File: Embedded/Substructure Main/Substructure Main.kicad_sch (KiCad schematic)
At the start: 12 parts, among them J1 M Pins, J2 C Pins, U1 G0 FFC, U2 G1 FFC, U3 S FFC

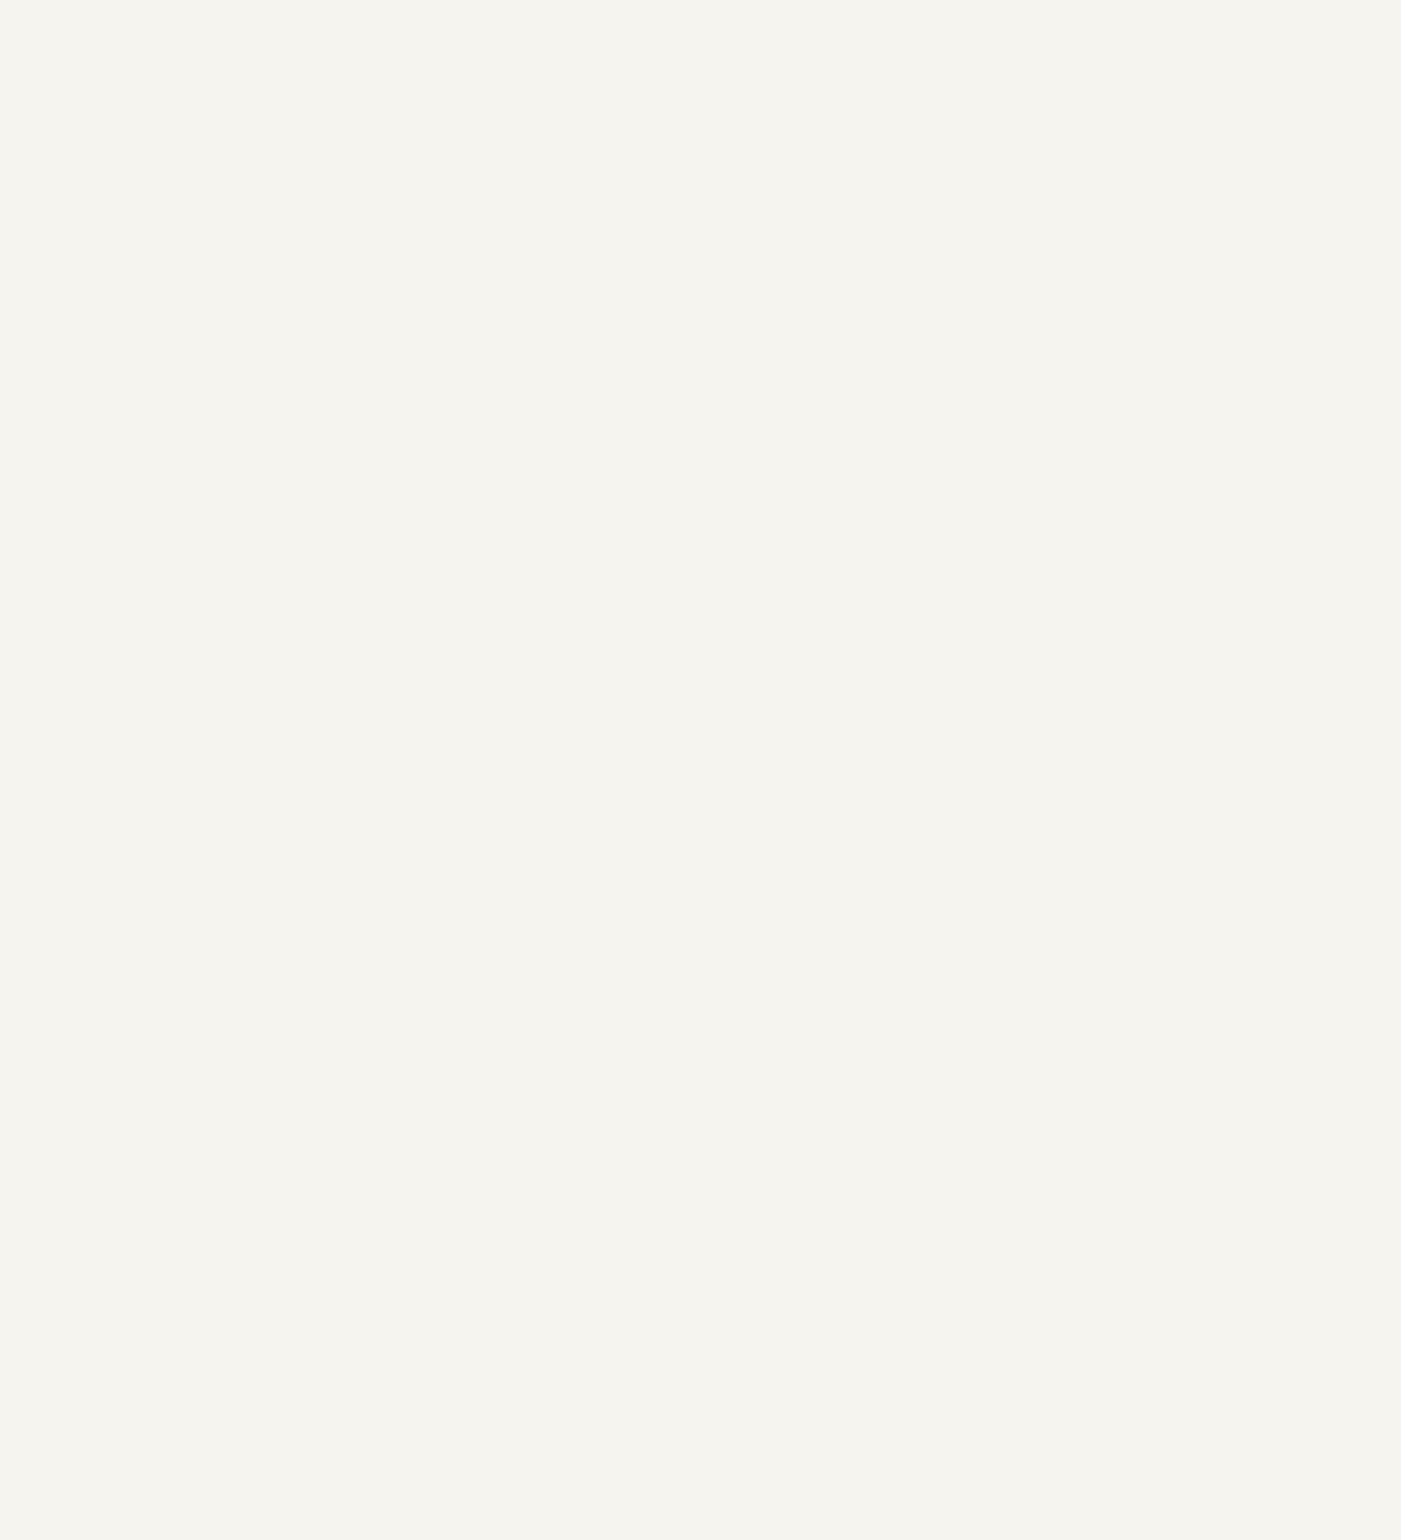
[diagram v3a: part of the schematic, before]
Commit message: Migrated Folders of KiCAD Files
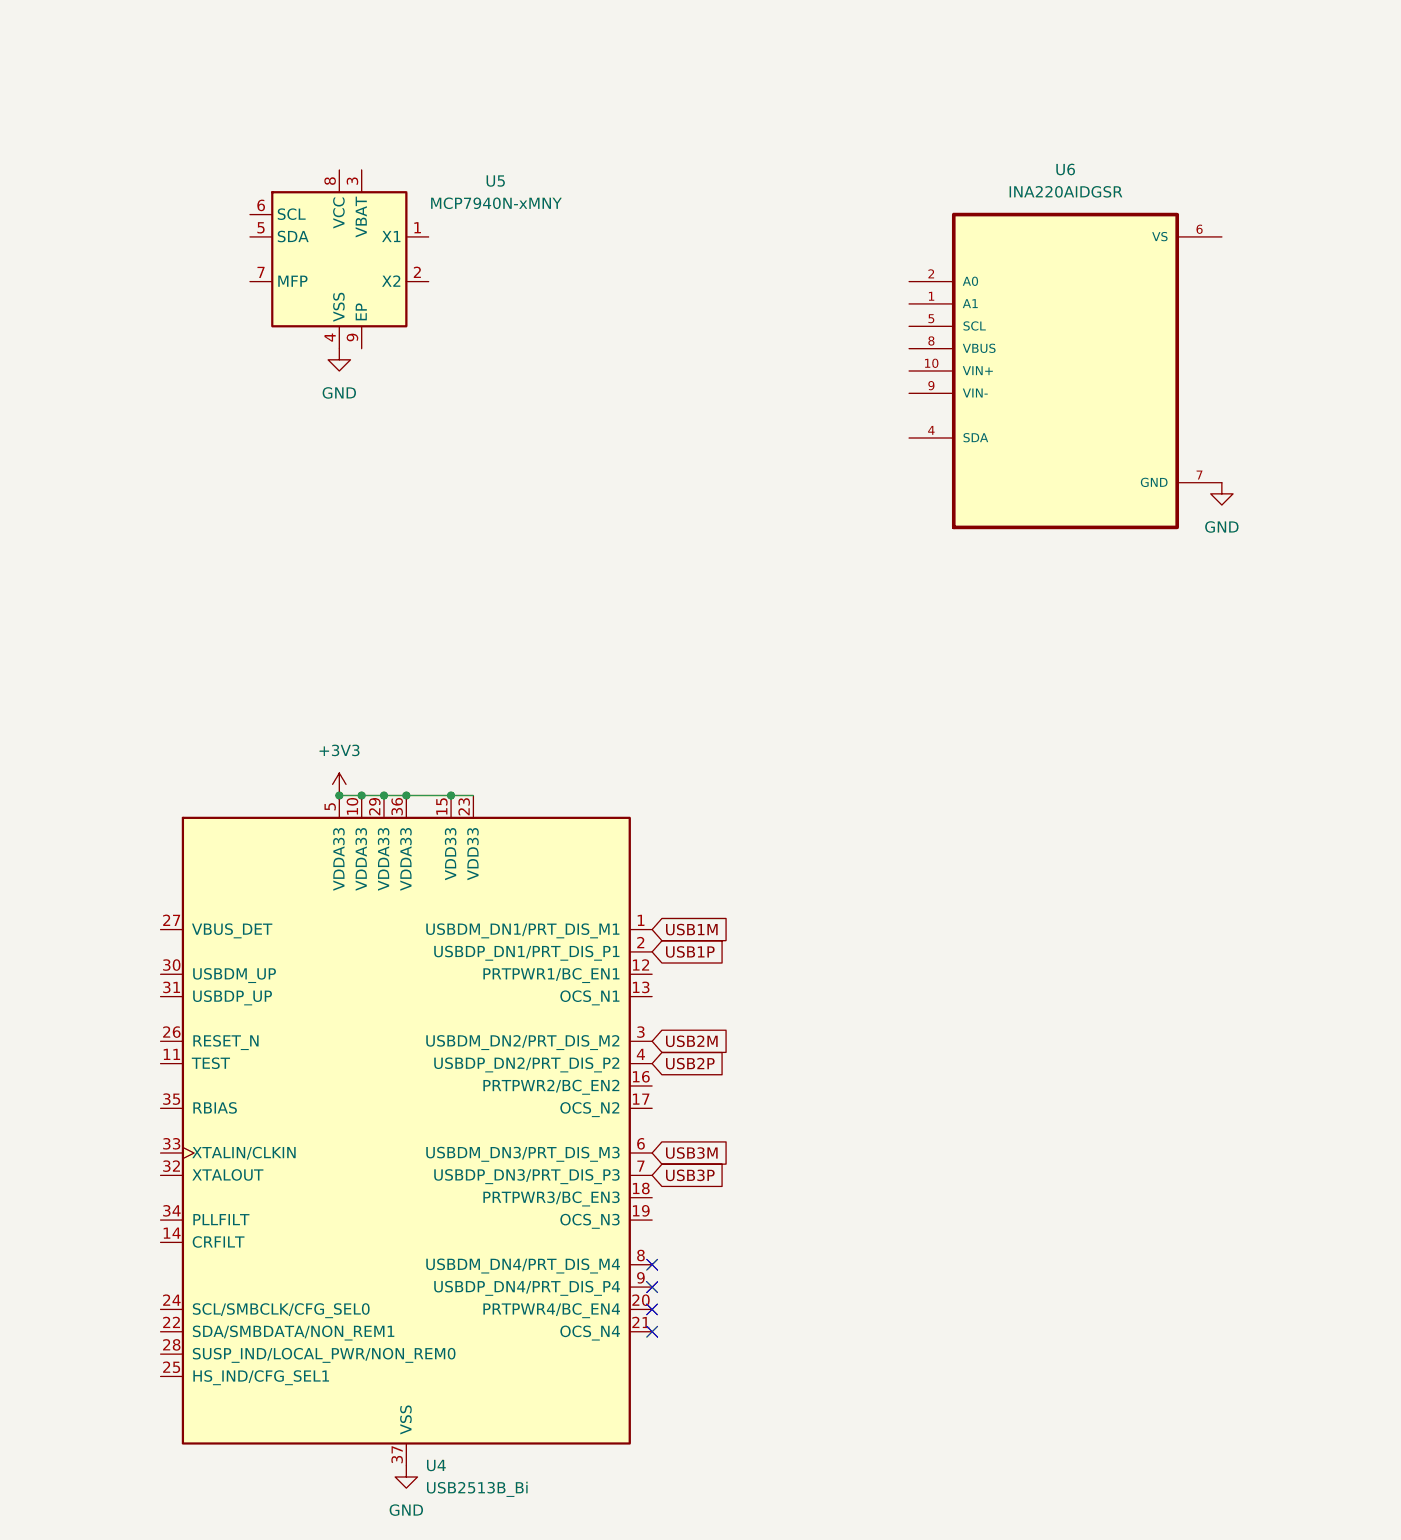
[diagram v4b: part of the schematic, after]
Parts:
- added U4: USB2513B_Bi, Package_DFN_QFN:QFN-36-1EP_6x6mm_P0.5mm_EP3.7x3.7mm, symbol Interface_USB:USB2514B_Bi
- added U5: MCP7940N-xMNY, Package_DFN_QFN:DFN-8-1EP_3x2mm_P0.5mm_EP1.36x1.46mm, symbol Timer_RTC:MCP7940N-xMNY
- added U6: INA220AIDGSR, INA220:SOP50P490X110-10N, symbol Current Sense:INA220AIDGSR
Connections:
- net +3V3: now also U4.10 (VDDA33), U4.15 (VDD33), U4.23 (VDD33), U4.29 (VDDA33), U4.36 (VDDA33), U4.5 (VDDA33)
- net GND: now also U4.37 (VSS), U5.4 (VSS), U6.7 (GND)
- new net USB1M: U4.1 (USBDM_DN1/PRT_DIS_M1)
- new net USB1P: U4.2 (USBDP_DN1/PRT_DIS_P1)
- new net USB2M: U4.3 (USBDM_DN2/PRT_DIS_M2)
- new net USB2P: U4.4 (USBDP_DN2/PRT_DIS_P2)
- new net USB3M: U4.6 (USBDM_DN3/PRT_DIS_M3)
- new net USB3P: U4.7 (USBDP_DN3/PRT_DIS_P3)
- no-connect marks 3 -> 7

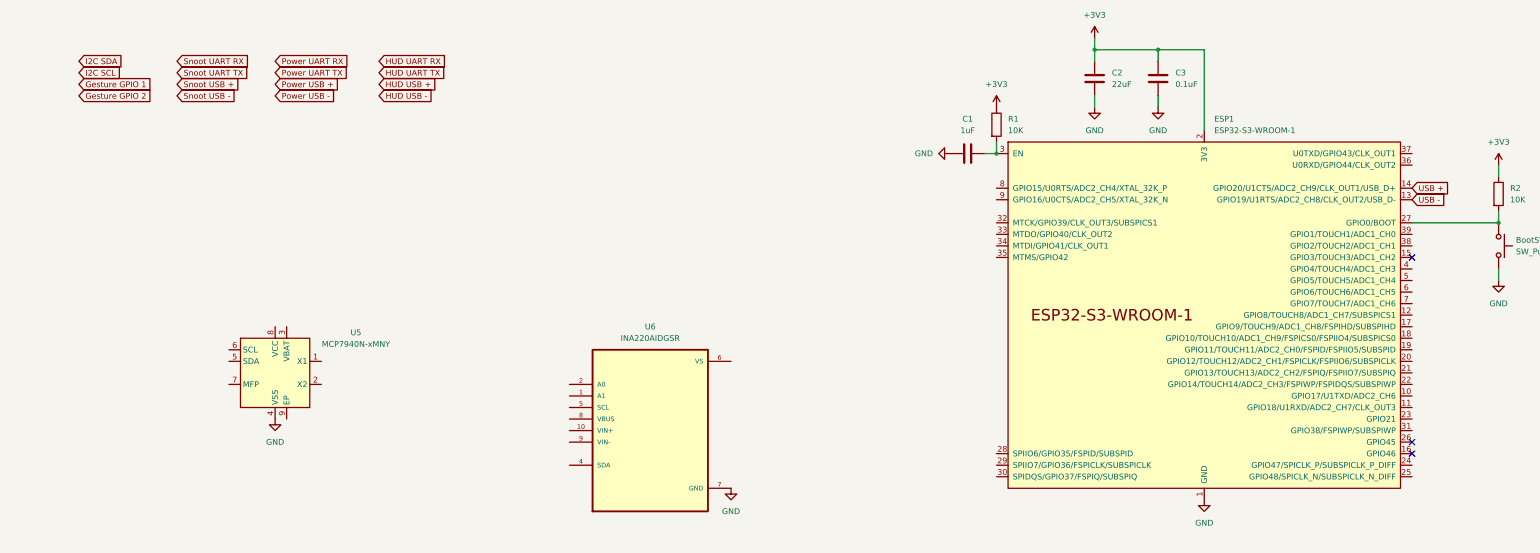
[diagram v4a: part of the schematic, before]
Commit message: Added USB & Power Pins for Main Board
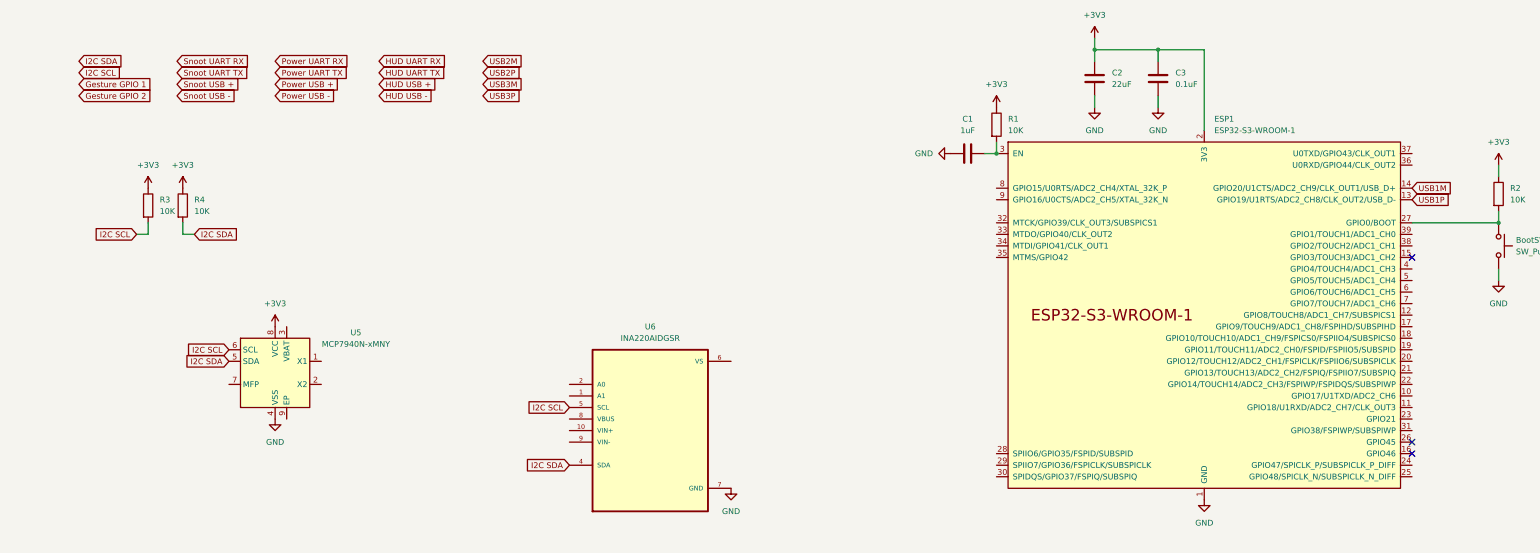
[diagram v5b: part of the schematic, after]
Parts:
- added R3, R4: 10K, Resistor_SMD:R_0603_1608Metric_Pad0.98x0.95mm_HandSolder, symbol Device:R
- ESP1: footprint PCM_Espressif:ESP32-S3-WROOM-1 -> RF_Module:ESP32-S3-WROOM-1
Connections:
- net USB + is gone; now on net USB1M: ESP1.14 (GPIO20/U1CTS/ADC2_CH9/CLK_OUT1/USB_D+)
- net USB - is gone; now on net USB1P: ESP1.13 (GPIO19/U1RTS/ADC2_CH8/CLK_OUT2/USB_D-)
- net +3V3: now also U5.8 (VCC), R3.1, R4.1
- net I2C SCL: now also U5.6 (SCL), U6.5 (SCL), R3.2
- net I2C SDA: now also U5.5 (SDA), U6.4 (SDA), R4.2

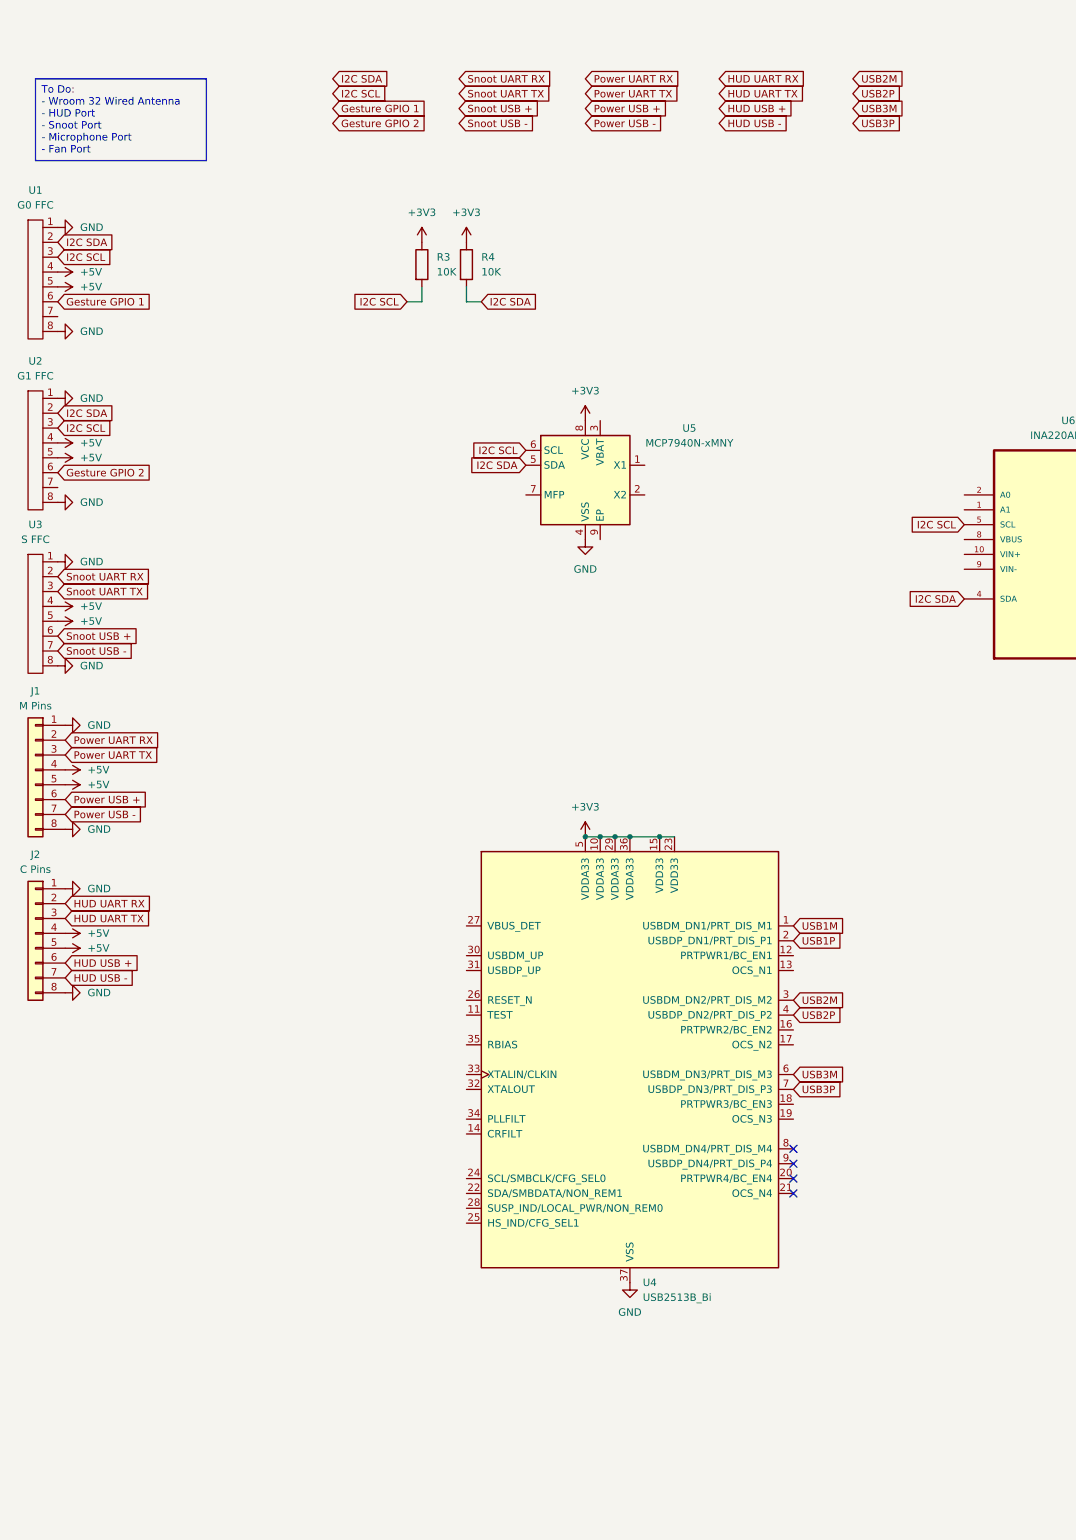
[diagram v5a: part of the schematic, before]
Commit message: Added Power Filtering and Connection for USB2513B_Bi
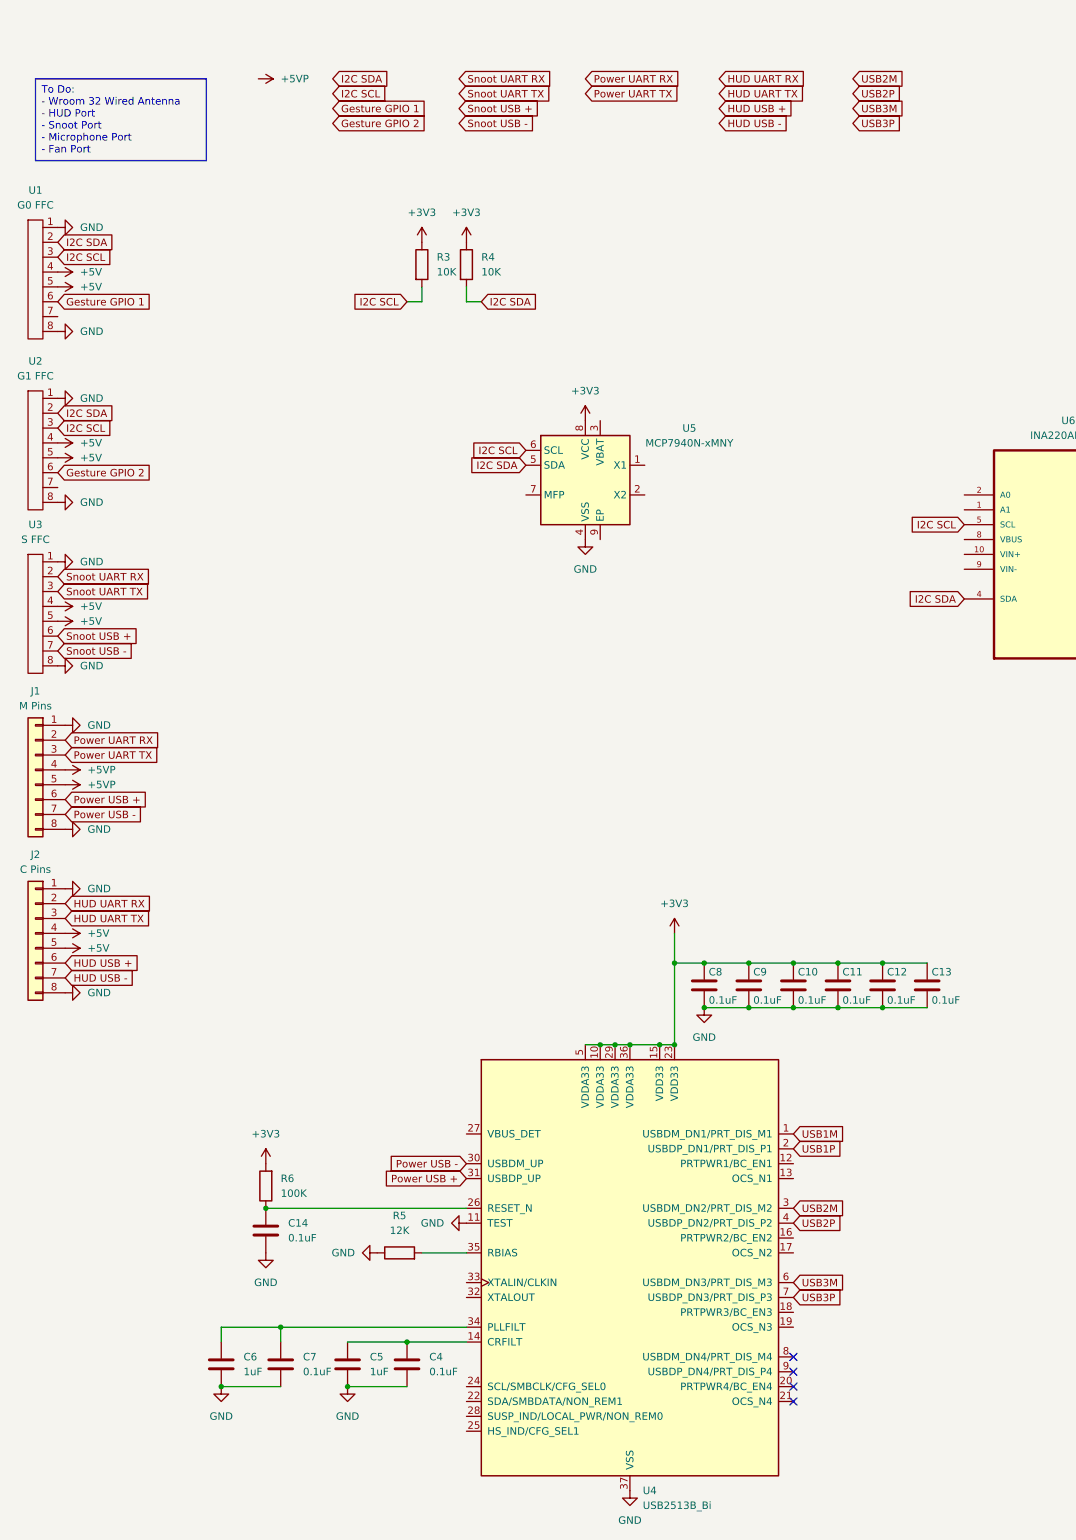
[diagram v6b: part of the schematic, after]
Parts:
- added C10, C11, C12, C13, C14, C4, C7, C8, C9: 0.1uF, Capacitor_SMD:C_0603_1608Metric_Pad1.08x0.95mm_HandSolder, symbol Device:C
- added C5, C6: 1uF, Capacitor_SMD:C_0603_1608Metric_Pad1.08x0.95mm_HandSolder, symbol Device:C
- added R5: 12K, Resistor_SMD:R_0603_1608Metric_Pad0.98x0.95mm_HandSolder, symbol Device:R
- added R6: 100K, Resistor_SMD:R_0603_1608Metric_Pad0.98x0.95mm_HandSolder, symbol Device:R
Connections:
- net +3V3: now also C10.1, C11.1, C12.1, C13.1, C8.1, C9.1, R6.2
- net +5V: no longer J1.4 (Pin_4), J1.5 (Pin_5)
- net GND: now also U4.11 (TEST), C10.2, C11.2, C12.2, C13.2, C14.2, C4.2, C5.2, C6.2, C7.2, C8.2, C9.2, R5.1
- net Power USB +: now also U4.31 (USBDP_UP)
- net Power USB -: now also U4.30 (USBDM_UP)
- net at U4.14 (CRFILT): now also C4.1, C5.1
- net at U4.26 (RESET_N): now also C14.1, R6.1
- net at U4.34 (PLLFILT): now also C6.1, C7.1
- net at U4.35 (RBIAS): now also R5.2
- new net +5VP: J1.4 (Pin_4), J1.5 (Pin_5)
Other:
- moved on the sheet: U4
